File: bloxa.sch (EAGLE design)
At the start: 92 parts, among them CON1 CON-4P-JST_GH-RA, CON2 CON-4P-JST_GH-RA, CON3 PINHEAD_1X02-2.54, IC1 MCP9700-SC70-5, IC2 TPD3S014DBVR-SOT23-6, IC3 TJA1051(X)/3-SO8, J1 CONNECTION, J2 CONNECTION, Q1 BUK9K6R2-40E,115, Q2 BUK9K6R2-40E,115, Q3 BUK9K6R2-40E,115

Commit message: Hardware files updated
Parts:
- removed CON3: PINHEAD_1X02-2.54, pinhead:PINHEAD_1X02-2.54
- added PAD47, PAD48: PAD-S-1.5, PADS:PAD-S-1.5
- D1: value PTVS36VP1UP,115-36V-SOD128 -> PTVS33VP1UTP,115-36V-SOD128; device TVS_diodes:PTVS36VP1UP,115-36V-SOD128 -> TVS_diodes:PTVS33VP1UTP,115-36V-SOD128
- LED1: device myxa_masterlib:LED-GREEN-0402 -> rc:LED-0402
- LED2: device myxa_masterlib:LED-GREEN-0402 -> rc:LED-0402; COLOR (none) -> GREEN; DIGIKEY# (none) -> 1830-IN-S42BT5GCT-ND; MANF (none) -> Inolux; MANF# (none) -> IN-S42BT5G
- LED3, LED4: device myxa_masterlib:LTST-C19HE1WT -> misc:LTST-C19HE1WT
- R10, R4: value 5 mOhms -> 10 mOhms; device SHUNT_RESISTORS:CURRENT_SHUNT_KELVIN-0.005R-2512-KELVIN -> SHUNT_RESISTORS:CURRENT_SHUNT_KELVIN-0.010R-2512-KELVIN
- R14: value 1K -> 680R; device R_digikey:1K-1%-0402 -> rc:R-1%-0402; AEC-Q (none) -> AEC-Q200; DIGIKEY# (none) -> CRCW0402680RFKEDDatasheet; MANF (none) -> Vishay Dale; MANF# (none) -> CRCW0402680RFKED
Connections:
- removed net N$2: IC3.S
- net GND: now also IC3.S, PAD47.P$1; no longer CON3.1
- net GPIO1: now also PAD48.P$1; no longer CON3.2
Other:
- note added: "-Current shunts replaced (5 mOhms replaced with 10 mOhms)- -Overcurrent protection added. Itrip is ~35 A -RCPWM th connector replaced with smd solder pads -Some design notes added to the schematic -TVS diode (D1) replaced with one that has lower breaksdown voltage"
- note added: "1.7"
- note added: "100"
- note added: "12"
- note added: "14.4"
- note added: "150"
- note added: "200"
- note added: "250"
- note added: "3"
- note added: "300"
- note added: "4.5"
- note added: "4.8"
- note added: "6.3"
- note added: "7.2"
- note added: "8.4"
- note added: "9.6"
- note added: "97.2"
- note added: "97.5"
- note added: "97.7"
- note added: "98"
- note added: "98.3"
- note added: "DC power, W"
- note added: "Efficiency, %"
- note added: "Phase current, I"
- note added: "Power losses for different power levels"
- note added: "R14 sets overcurrent protection trip level. 680R sets ir arount 35A, which is 2.5 times higher than maximum phase current for 300W DC power when running on discharged 8S battery"
- note added: "The table is valid for 26.4 V supply voltage which is the same as a discharched 8S Li-ion battery"
- note added: "Total losses, W"
- note removed: "https://www.digikey.com/product-detail/en/united-chemi-con/EKZN500ELL181MH20D/565-4066-ND/4843876"

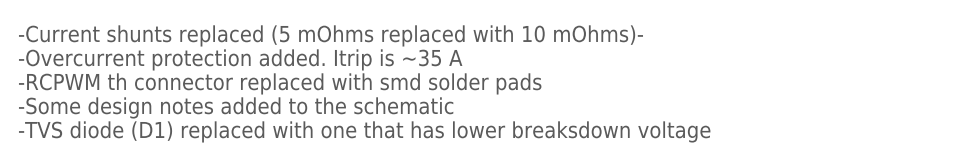
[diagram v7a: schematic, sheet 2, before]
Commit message: Update bloxa.sch
Typo
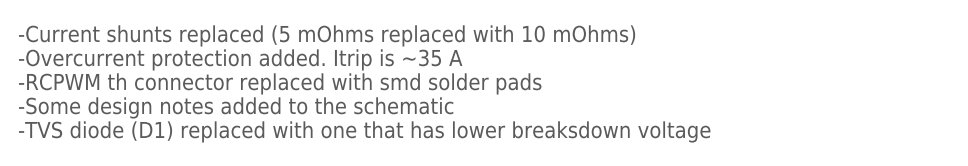
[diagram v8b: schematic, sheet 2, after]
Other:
- note added: "-Current shunts replaced (5 mOhms replaced with 10 mOhms) -Overcurrent protection added. Itrip is ~35 A -RCPWM th connector replaced with smd solder pads -Some design notes added to the schematic -TVS diode (D1) replaced with one that has lower breaksdown voltage"
- note removed: "-Current shunts replaced (5 mOhms replaced with 10 mOhms)- -Overcurrent protection added. Itrip is ~35 A -RCPWM th connector replaced with smd solder pads -Some design notes added to the schematic -TVS diode (D1) replaced with one that has lower breaksdown voltage"
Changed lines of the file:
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@@
 <?xml version="1.0" encoding="utf-8"?>
 <!DOCTYPE eagle SYSTEM "eagle.dtd">
-<eagle version="9.6.1">
+<eagle version="9.6.2">
 <drawing>
 <settings>
@@
 <description>changelog</description>
 <plain>
-<text x="7.62" y="124.46" size="1.778" layer="97" font="vector" align="top-left">-Current shunts replaced (5 mOhms replaced with 10 mOhms)-
+<text x="7.62" y="124.46" size="1.778" layer="97" font="vector" align="top-left">-Current shunts replaced (5 mOhms replaced with 10 mOhms)
 -Overcurrent protection added. Itrip is ~35 A
 -RCPWM th connector replaced with smd solder pads
